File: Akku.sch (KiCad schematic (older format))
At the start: 45 parts, among them J1 +/- Stecker, J2 load/up, J3 down/en/clear, P7 CONN_02X10, P8 CONN_02X10, P9 CONN_02X10, SW1 UP_Bonsai_SWITCH_INV, SW2 DOWN_Bonsai_SWITCH_INV, SW3 CLR_Bonsai_SWITCH_INV, U1 74HC14, U2 7400, U4 7408, U5 74LS193, U6 74LS541, U7 74LS193, U8 74LS540

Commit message: akku sch updates for same wireing in pcb
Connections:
- net labels added: CLR, ^down, ^enable, ^load, ûp
- wire segments 226 -> 245
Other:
- moved on the sheet: D1, J2, J3, R9

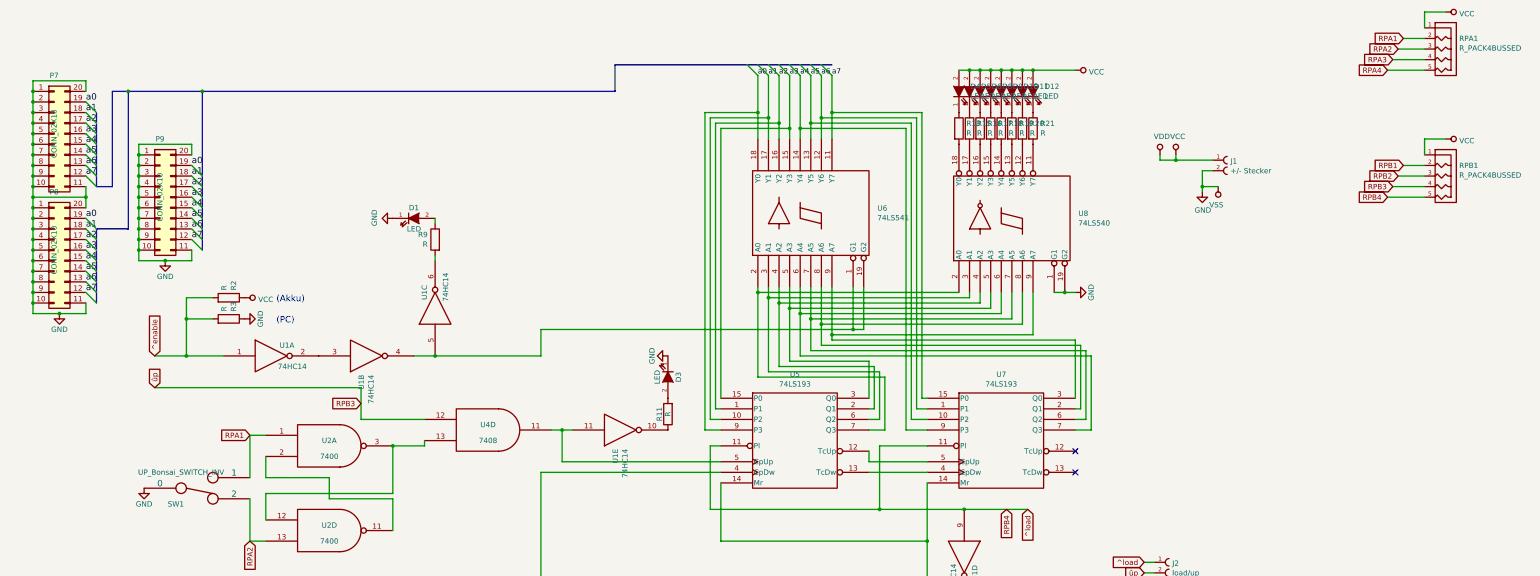
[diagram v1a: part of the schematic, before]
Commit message: akku wireing in pcb
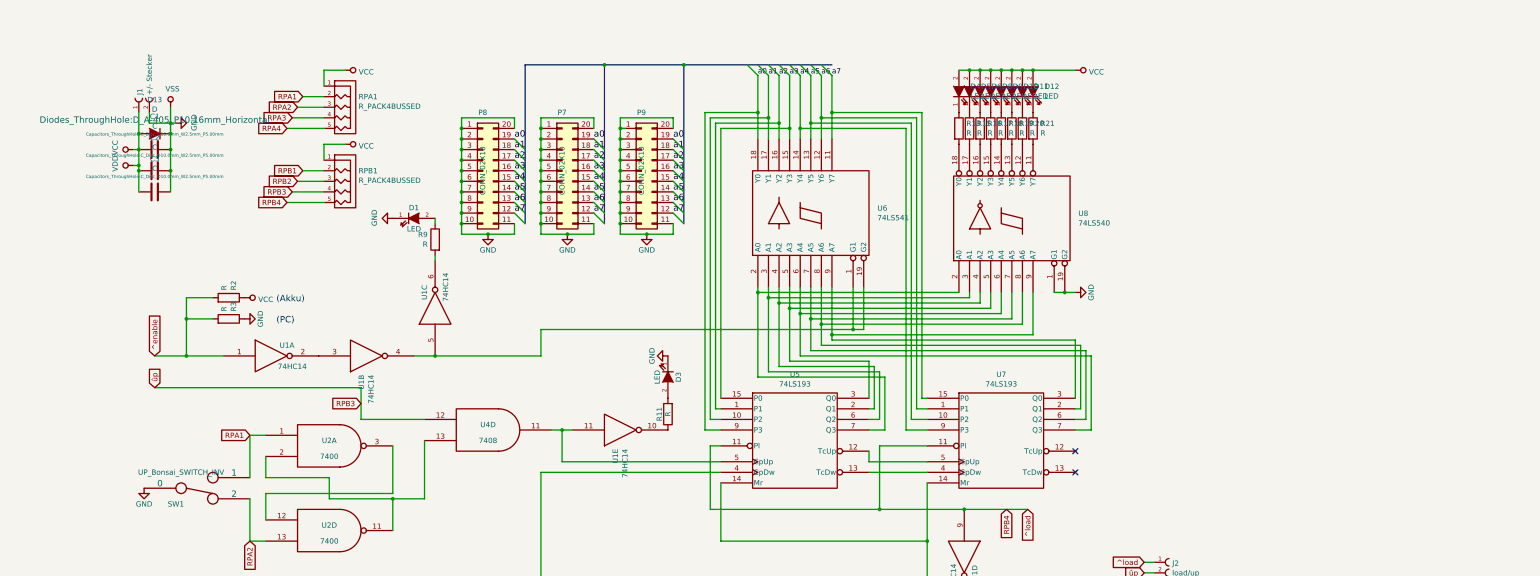
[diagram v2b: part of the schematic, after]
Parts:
- added C1, C2, C3: C, Capacitors_ThroughHole:C_Disc_D10.0mm_W2.5mm_P5.00mm, symbol bonsai:C
- added D13: D, Diodes_ThroughHole:D_A-405_P10.16mm_Horizontal, symbol bonsai:D
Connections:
- net GND: now also C1.1, C2.1, C3.1, D13.1 (K)
- net VCC: now also C1.2, C2.2, C3.2, D13.2 (A)
- net at U2.12, U2.3: no longer U4.13
- net at U2.11, U2.2: now also U4.13
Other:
- moved on the sheet: J1, P7, P8, P9, RPA1, RPB1

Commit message: akku and wireing in pcb
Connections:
- net GND: now also SW3.6
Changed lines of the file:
@@
 Connection ~ 850  1600
 Connection ~ 1150 1600
+$Comp
+L power:GND #PWR?
+U 1 1 5CDAAA47
+P 8000 5950
+F 0 "#PWR?" H 8000 5700 50  0001 C CNN
+F 1 "GND" H 8000 5800 50  0000 C CNN
+F 2 "" H 8000 5950 50  0000 C CNN
+F 3 "" H 8000 5950 50  0000 C CNN
+	1    8000 5950
+	0    -1   -1   0
+$EndComp
 Wire Bus Line
 	5250 600  5250 2100

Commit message: Akku pc finished
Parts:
- C1, C2, C3: footprint Capacitors_ThroughHole:C_Disc_D10.0mm_W2.5mm_P5.00mm -> tg_foodprint:C_Disc_D10.0mm_W2.5mm_P5.00mm
- D13: footprint Diodes_ThroughHole:D_A-405_P10.16mm_Horizontal -> Pin_Headers:D_DO-41_SOD81_P10.16mm_Horizontal
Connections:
- net at U5.12 (TcUp): no longer U7.5 (CpUp)
- net at U5.13 (TcDw): no longer U7.4 (CpDw)
- net at U1.13, U4.3: now also U7.4 (CpDw); no longer U5.4 (CpDw)
- net at U1.11, U4.11: now also U7.5 (CpUp); no longer U5.5 (CpUp)
- net at U7.12 (TcUp): now also U5.5 (CpUp)
- net at U7.13 (TcDw): now also U5.4 (CpDw)
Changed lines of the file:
@@
 Wire Wire Line
 	8300 4550 8300 5100
-Wire Wire Line
-	4650 4450 6350 4450
 Connection ~ 4650 6050
-Wire Wire Line
-	4650 4450 4650 6050
 Wire Wire Line
 	4600 6050 4650 6050
@@
 	8300 5100 6350 5100
 Wire Wire Line
-	7750 4350 7750 4250
-Wire Wire Line
-	8300 4350 7750 4350
-Wire Wire Line
 	6250 4200 6350 4200
 Wire Wire Line
@@
 Wire Wire Line
 	7300 2700 7300 3050
-Wire Wire Line
-	7750 4450 8300 4450
-NoConn ~ 9700 4250
-NoConn ~ 9700 4450
 $Comp
 L Akku-rescue:74HC14-RESCUE-Akku U1
@@
 Connection ~ 9600 2750
 Wire Wire Line
-	6350 4350 4850 4350
-Wire Wire Line
-	4850 4350 4850 4050
+	6350 4350 6050 4350
 Connection ~ 4850 4050
 Wire Wire Line
@@
 F 0 "C1" V 688 1400 50  0000 C CNN
 F 1 "C" V 779 1400 50  0000 C CNN
-F 2 "Capacitors_ThroughHole:C_Disc_D10.0mm_W2.5mm_P5.00mm" V 855 1400 30  0000 C CNN
+F 2 "tg_foodprint:C_Disc_D10.0mm_W2.5mm_P5.00mm" V 855 1400 30  0000 C CNN
 F 3 "" H 1000 1400 60  0000 C CNN
 	1    1000 1400
@@
 F 0 "C2" V 688 1600 50  0000 C CNN
 F 1 "C" V 779 1600 50  0000 C CNN
-F 2 "Capacitors_ThroughHole:C_Disc_D10.0mm_W2.5mm_P5.00mm" V 855 1600 30  0000 C CNN
+F 2 "tg_foodprint:C_Disc_D10.0mm_W2.5mm_P5.00mm" V 855 1600 30  0000 C CNN
 F 3 "" H 1000 1600 60  0000 C CNN
 	1    1000 1600
@@
 F 0 "D13" H 1000 929 50  0000 C CNN
 F 1 "D" H 1000 1020 50  0000 C CNN
-F 2 "Diodes_ThroughHole:D_A-405_P10.16mm_Horizontal" H 1000 1119 60  0000 C CNN
+F 2 "Pin_Headers:D_DO-41_SOD81_P10.16mm_Horizontal" H 1000 1119 60  0000 C CNN
 F 3 "" H 1000 1250 60  0000 C CNN
 	1    1000 1250
@@
 F 0 "C3" V 688 1800 50  0000 C CNN
 F 1 "C" V 779 1800 50  0000 C CNN
-F 2 "Capacitors_ThroughHole:C_Disc_D10.0mm_W2.5mm_P5.00mm" V 855 1800 30  0000 C CNN
+F 2 "tg_foodprint:C_Disc_D10.0mm_W2.5mm_P5.00mm" V 855 1800 30  0000 C CNN
 F 3 "" H 1000 1800 60  0000 C CNN
 	1    1000 1800
@@
 Connection ~ 1150 1600
 $Comp
-L power:GND #PWR?
+L power:GND #PWR0104
 U 1 1 5CDAAA47
 P 8000 5950
-F 0 "#PWR?" H 8000 5700 50  0001 C CNN
+F 0 "#PWR0104" H 8000 5700 50  0001 C CNN
 F 1 "GND" H 8000 5800 50  0000 C CNN
 F 2 "" H 8000 5950 50  0000 C CNN
@@
 	0    -1   -1   0
 $EndComp
+Wire Wire Line
+	9700 4450 9700 4650
+Wire Wire Line
+	9700 4650 6100 4650
+Wire Wire Line
+	6100 4650 6100 4450
+Wire Wire Line
+	9700 4250 9800 4250
+Wire Wire Line
+	9800 4250 9800 4700
+Wire Wire Line
+	8300 4450 8150 4450
+Wire Wire Line
+	8150 4450 8150 5350
+Wire Wire Line
+	8150 5350 4650 5350
+Wire Wire Line
+	4650 5350 4650 6050
+Wire Wire Line
+	6050 4700 6050 4350
+Wire Wire Line
+	9800 4700 6050 4700
+Wire Wire Line
+	8300 4350 8100 4350
+Wire Wire Line
+	8100 4350 8100 5250
+Wire Wire Line
+	8100 5250 4850 5250
+Wire Wire Line
+	4850 4050 4850 5250
+NoConn ~ 7750 4250
+NoConn ~ 7750 4450
+Wire Wire Line
+	6350 4450 6100 4450
+Wire Bus Line
+	6000 600  7400 600
+Wire Bus Line
+	4500 600  4500 2100
 Wire Bus Line
 	5250 600  5250 2100
 Wire Bus Line
-	4500 600  4500 2100
-Wire Bus Line
 	6000 600  6000 2100
-Wire Bus Line
-	6000 600  7400 600
 $EndSCHEMATC

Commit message: Eintakt libs fixed
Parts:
- C1, C2, C3: symbol bonsai:C -> Akku-rescue:C-bonsai-Akku-rescue
- D1, D10, D11, D12, D2, D3, D4, D5, D6, D7, D8, D9: symbol bonsai:LED -> Akku-rescue:LED-bonsai-Akku-rescue
- D13: symbol bonsai:D -> Akku-rescue:D-bonsai-Akku-rescue
- J1, J2: symbol Akku-rescue:2PinTerminalBlocktg-2PinTerminalBlocktg -> Akku-rescue:2PinTerminalBlocktg-2PinTerminalBlocktg-Akku-rescue-Akku-rescue
- J3: symbol Akku-rescue:3PinTerminalBlocktg-3PinTerminalBlocktg -> Akku-rescue:3PinTerminalBlocktg-3PinTerminalBlocktg-Akku-rescue-Akku-rescue
- P7, P8, P9: symbol Akku-rescue:Conn_02x10_Counter_Clockwise-conn -> Akku-rescue:Conn_02x10_Counter_Clockwise-conn-Akku-rescue-Akku-rescue
- R10, R11, R12, R13, R14, R15, R16, R17, R18, R19, R2, R20, R21, R3, R9: symbol Akku-rescue:R-device -> Akku-rescue:R-device-Akku-rescue-Akku-rescue
- RPA1, RPB1: symbol bonsai:R_PACK4BUSSED -> Akku-rescue:R_PACK4BUSSED-bonsai-Akku-rescue
- SW1, SW2, SW3: symbol bonsai:SWITCH_INV -> Akku-rescue:SWITCH_INV-bonsai-Akku-rescue
- U1: symbol Akku-rescue:4069-cmos4000 -> Akku-rescue:4069-cmos4000-Akku-rescue-Akku-rescue
- U1: symbol Akku-rescue:74HC14-RESCUE-Akku -> Akku-rescue:74HC14-RESCUE-Akku-Akku-rescue-Akku-rescue
- U2: symbol Akku-rescue:7400-RESCUE-Akku -> Akku-rescue:7400-RESCUE-Akku-Akku-rescue-Akku-rescue
- U4: symbol Akku-rescue:74LS08-74xx -> Akku-rescue:74LS08-74xx-Akku-rescue-Akku-rescue
- U5, U7: symbol Akku-rescue:74LS193-RESCUE-Akku -> Akku-rescue:74LS193-RESCUE-Akku-Akku-rescue-Akku-rescue
- U6: symbol Akku-rescue:74LS541-74xx -> Akku-rescue:74LS541-74xx-Akku-rescue-Akku-rescue
- U8: symbol Akku-rescue:74LS540-74xx -> Akku-rescue:74LS540-74xx-Akku-rescue-Akku-rescue
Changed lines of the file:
@@
 Akkumulator
 $Comp
-L Akku-rescue:74LS540-74xx U8
+L Akku-rescue:74LS540-74xx-Akku-rescue-Akku-rescue U8
 U 1 1 57E93AAD
 P 9100 2050
@@
 $EndComp
 $Comp
-L bonsai:LED D12
+L Akku-rescue:LED-bonsai-Akku-rescue D12
 U 1 1 57E93BF0
 P 9300 850
@@
 $EndComp
 $Comp
-L bonsai:LED D11
+L Akku-rescue:LED-bonsai-Akku-rescue D11
 U 1 1 57E93CED
 P 9200 850
@@
 $EndComp
 $Comp
-L bonsai:LED D10
+L Akku-rescue:LED-bonsai-Akku-rescue D10
 U 1 1 57E93ED1
 P 9100 850
@@
 $EndComp
 $Comp
-L bonsai:LED D9
+L Akku-rescue:LED-bonsai-Akku-rescue D9
 U 1 1 57E93F38
 P 9000 850
@@
 $EndComp
 $Comp
-L bonsai:LED D8
+L Akku-rescue:LED-bonsai-Akku-rescue D8
 U 1 1 57E93F7E
 P 8900 850
@@
 $EndComp
 $Comp
-L bonsai:LED D6
+L Akku-rescue:LED-bonsai-Akku-rescue D6
 U 1 1 57E93FA3
 P 8800 850
@@
 $EndComp
 $Comp
-L bonsai:LED D5
+L Akku-rescue:LED-bonsai-Akku-rescue D5
 U 1 1 57E93FCF
 P 8700 850
@@
 $EndComp
 $Comp
-L bonsai:LED D4
+L Akku-rescue:LED-bonsai-Akku-rescue D4
 U 1 1 57E93FFA
 P 8600 850
@@
 $EndComp
 $Comp
-L Akku-rescue:R-device R13
+L Akku-rescue:R-device-Akku-rescue-Akku-rescue R13
 U 1 1 57E94162
 P 8600 1200
@@
 $EndComp
 $Comp
-L Akku-rescue:R-device R15
+L Akku-rescue:R-device-Akku-rescue-Akku-rescue R15
 U 1 1 57E942DE
 P 8700 1200
@@
 $EndComp
 $Comp
-L Akku-rescue:R-device R16
+L Akku-rescue:R-device-Akku-rescue-Akku-rescue R16
 U 1 1 57E94316
 P 8800 1200
@@
 $EndComp
 $Comp
-L Akku-rescue:R-device R17
+L Akku-rescue:R-device-Akku-rescue-Akku-rescue R17
 U 1 1 57E94362
 P 8900 1200
@@
 $EndComp
 $Comp
-L Akku-rescue:R-device R18
+L Akku-rescue:R-device-Akku-rescue-Akku-rescue R18
 U 1 1 57E943BA
 P 9000 1200
@@
 $EndComp
 $Comp
-L Akku-rescue:R-device R19
+L Akku-rescue:R-device-Akku-rescue-Akku-rescue R19
 U 1 1 57E94424
 P 9100 1200
@@
 $EndComp
 $Comp
-L Akku-rescue:R-device R20
+L Akku-rescue:R-device-Akku-rescue-Akku-rescue R20
 U 1 1 57E94464
 P 9200 1200
@@
 $EndComp
 $Comp
-L Akku-rescue:R-device R21
+L Akku-rescue:R-device-Akku-rescue-Akku-rescue R21
 U 1 1 57E944B7
 P 9300 1200
@@
 $EndComp
 $Comp
-L Akku-rescue:74LS193-RESCUE-Akku U5
+L Akku-rescue:74LS193-RESCUE-Akku-Akku-rescue-Akku-rescue U5
 U 1 1 57E9530E
 P 7050 4150
@@
 $EndComp
 $Comp
-L Akku-rescue:74LS193-RESCUE-Akku U7
+L Akku-rescue:74LS193-RESCUE-Akku-Akku-rescue-Akku-rescue U7
 U 1 1 57E95727
 P 9000 4150
@@
 $EndComp
 $Comp
-L Akku-rescue:R-device R14
+L Akku-rescue:R-device-Akku-rescue-Akku-rescue R14
 U 1 1 57E98213
 P 8650 5850
@@
 $EndComp
 $Comp
-L Akku-rescue:R-device R9
+L Akku-rescue:R-device-Akku-rescue-Akku-rescue R9
 U 1 1 57F2FBEB
 P 3650 2250
@@
 $EndComp
 $Comp
-L bonsai:LED D7
+L Akku-rescue:LED-bonsai-Akku-rescue D7
 U 1 1 57FBC65C
 P 8850 6000
@@
 $EndComp
 $Comp
-L Akku-rescue:R-device R12
+L Akku-rescue:R-device-Akku-rescue-Akku-rescue R12
 U 1 1 57FC1E29
 P 8150 6200
@@
 $EndComp
 $Comp
-L bonsai:SWITCH_INV SW3
+L Akku-rescue:SWITCH_INV-bonsai-Akku-rescue SW3
 U 1 1 57FC34DF
 P 7500 6200
@@
 $EndComp
 $Comp
-L Akku-rescue:74LS541-74xx U6
+L Akku-rescue:74LS541-74xx-Akku-rescue-Akku-rescue U6
 U 1 1 57E939A0
 P 7200 2000
@@
 $EndComp
 $Comp
-L Akku-rescue:Conn_02x10_Counter_Clockwise-conn P7
+L Akku-rescue:Conn_02x10_Counter_Clockwise-conn-Akku-rescue-Akku-rescue P7
 U 1 1 58057A43
 P 4850 1600
@@
 $EndComp
 $Comp
-L Akku-rescue:Conn_02x10_Counter_Clockwise-conn P8
+L Akku-rescue:Conn_02x10_Counter_Clockwise-conn-Akku-rescue-Akku-rescue P8
 U 1 1 5805867B
 P 4100 1600
@@
 $EndComp
 $Comp
-L Akku-rescue:Conn_02x10_Counter_Clockwise-conn P9
+L Akku-rescue:Conn_02x10_Counter_Clockwise-conn-Akku-rescue-Akku-rescue P9
 U 1 1 58058F42
 P 5600 1600
@@
 $EndComp
 $Comp
-L bonsai:LED D1
+L Akku-rescue:LED-bonsai-Akku-rescue D1
 U 1 1 580EE5C2
 P 3450 2050
@@
 $EndComp
 $Comp
-L Akku-rescue:4069-cmos4000 U1
+L Akku-rescue:4069-cmos4000-Akku-rescue-Akku-rescue U1
 U 2 1 580F11C5
 P 3000 3350
@@
 $EndComp
 $Comp
-L Akku-rescue:R-device R2
+L Akku-rescue:R-device-Akku-rescue-Akku-rescue R2
 U 1 1 580F178A
 P 1700 2800
@@
 $EndComp
 $Comp
-L Akku-rescue:R-device R3
+L Akku-rescue:R-device-Akku-rescue-Akku-rescue R3
 U 1 1 580F350E
 P 1700 3000
@@
 (PC)
 $Comp
-L Akku-rescue:74LS08-74xx U4
+L Akku-rescue:74LS08-74xx-Akku-rescue-Akku-rescue U4
 U 4 1 580F517F
 P 4150 4050
@@
 $EndComp
 $Comp
-L Akku-rescue:7400-RESCUE-Akku U2
+L Akku-rescue:7400-RESCUE-Akku-Akku-rescue-Akku-rescue U2
 U 4 1 580F5956
 P 2650 5000
@@
 $EndComp
 $Comp
-L Akku-rescue:7400-RESCUE-Akku U2
+L Akku-rescue:7400-RESCUE-Akku-Akku-rescue-Akku-rescue U2
 U 1 1 580F5818
 P 2650 4200
@@
 $EndComp
 $Comp
-L bonsai:SWITCH_INV SW1
+L Akku-rescue:SWITCH_INV-bonsai-Akku-rescue SW1
 U 1 1 58100CBF
 P 1400 4600
@@
 $EndComp
 $Comp
-L Akku-rescue:4069-cmos4000 U1
+L Akku-rescue:4069-cmos4000-Akku-rescue-Akku-rescue U1
 U 5 1 581014B6
 P 5400 4050
@@
 $EndComp
 $Comp
-L Akku-rescue:R-device R11
+L Akku-rescue:R-device-Akku-rescue-Akku-rescue R11
 U 1 1 581018B2
 P 5850 3900
@@
 $EndComp
 $Comp
-L bonsai:LED D3
+L Akku-rescue:LED-bonsai-Akku-rescue D3
 U 1 1 58101E2D
 P 5850 3550
@@
 $EndComp
 $Comp
-L Akku-rescue:7400-RESCUE-Akku U2
+L Akku-rescue:7400-RESCUE-Akku-Akku-rescue-Akku-rescue U2
 U 3 1 58103E9D
 P 2650 5950
@@
 $EndComp
 $Comp
-L Akku-rescue:7400-RESCUE-Akku U2
+L Akku-rescue:7400-RESCUE-Akku-Akku-rescue-Akku-rescue U2
 U 2 1 58103EA3
 P 2650 6750
@@
 $EndComp
 $Comp
-L bonsai:SWITCH_INV SW2
+L Akku-rescue:SWITCH_INV-bonsai-Akku-rescue SW2
 U 1 1 58103EB5
 P 1400 6350
@@
 $EndComp
 $Comp
-L Akku-rescue:74LS08-74xx U4
+L Akku-rescue:74LS08-74xx-Akku-rescue-Akku-rescue U4
 U 1 1 581052DF
 P 4000 6050
@@
 	7300 2700 7300 3050
 $Comp
-L Akku-rescue:74HC14-RESCUE-Akku U1
+L Akku-rescue:74HC14-RESCUE-Akku-Akku-rescue-Akku-rescue U1
 U 1 1 5A159C74
 P 2100 3350
@@
 $EndComp
 $Comp
-L Akku-rescue:74HC14-RESCUE-Akku U1
+L Akku-rescue:74HC14-RESCUE-Akku-Akku-rescue-Akku-rescue U1
 U 3 1 5A159ED2
 P 3650 2900
@@
 $EndComp
 $Comp
-L Akku-rescue:74HC14-RESCUE-Akku U1
+L Akku-rescue:74HC14-RESCUE-Akku-Akku-rescue-Akku-rescue U1
 U 6 1 5A15A24E
 P 5200 6050
@@
 $EndComp
 $Comp
-L Akku-rescue:74HC14-RESCUE-Akku U1
+L Akku-rescue:74HC14-RESCUE-Akku-Akku-rescue-Akku-rescue U1
 U 4 1 5A15A4DE
 P 8650 5250
@@
 	850  1400 800  1400
 $Comp
-L Akku-rescue:2PinTerminalBlocktg-2PinTerminalBlocktg J1
+L Akku-rescue:2PinTerminalBlocktg-2PinTerminalBlocktg-Akku-rescue-Akku-rescue J1
 U 1 1 5AECBED9
 P 850 850
@@
 $EndComp
 $Comp
-L Akku-rescue:2PinTerminalBlocktg-2PinTerminalBlocktg J2
+L Akku-rescue:2PinTerminalBlocktg-2PinTerminalBlocktg-Akku-rescue-Akku-rescue J2
 U 1 1 5AECC155
 P 10650 5300
@@
 $EndComp
 $Comp
-L Akku-rescue:3PinTerminalBlocktg-3PinTerminalBlocktg J3
+L Akku-rescue:3PinTerminalBlocktg-3PinTerminalBlocktg-Akku-rescue-Akku-rescue J3
 U 1 1 5AECC360
 P 10650 5650
@@
 	1150 1150 1200 1150
 $Comp
-L bonsai:R_PACK4BUSSED RPA1
+L Akku-rescue:R_PACK4BUSSED-bonsai-Akku-rescue RPA1
 U 1 1 5B220C3D
 P 2800 1000
@@
 $EndComp
 $Comp
-L Akku-rescue:R-device R10
+L Akku-rescue:R-device-Akku-rescue-Akku-rescue R10
 U 1 1 5810516E
 P 5650 6200
@@
 $EndComp
 $Comp
-L bonsai:LED D2
+L Akku-rescue:LED-bonsai-Akku-rescue D2
 U 1 1 58105174
 P 5650 6550
@@
 RPA3
 $Comp
-L bonsai:R_PACK4BUSSED RPB1
+L Akku-rescue:R_PACK4BUSSED-bonsai-Akku-rescue RPB1
 U 1 1 5B22DE13
 P 2800 1700
@@
 Connection ~ 6000 600
 $Comp
-L bonsai:C C1
+L Akku-rescue:C-bonsai-Akku-rescue C1
 U 1 1 5CBF3D2E
 P 1000 1400
 F 0 "C1" V 688 1400 50  0000 C CNN
 F 1 "C" V 779 1400 50  0000 C CNN
-F 2 "tg_foodprint:C_Disc_D10.0mm_W2.5mm_P5.00mm" V 855 1400 30  0000 C CNN
+F 2 "tg_foodprint:C_Disc_D10.0mm_W2.5mm_P5.00mm" V 855 1400 30  0001 C CNN
 F 3 "" H 1000 1400 60  0000 C CNN
 	1    1000 1400
@@
 $EndComp
 $Comp
-L bonsai:C C2
+L Akku-rescue:C-bonsai-Akku-rescue C2
 U 1 1 5CBF52E5
 P 1000 1600
 F 0 "C2" V 688 1600 50  0000 C CNN
 F 1 "C" V 779 1600 50  0000 C CNN
-F 2 "tg_foodprint:C_Disc_D10.0mm_W2.5mm_P5.00mm" V 855 1600 30  0000 C CNN
+F 2 "tg_foodprint:C_Disc_D10.0mm_W2.5mm_P5.00mm" V 855 1600 30  0001 C CNN
 F 3 "" H 1000 1600 60  0000 C CNN
 	1    1000 1600
@@
 $EndComp
 $Comp
-L bonsai:D D13
+L Akku-rescue:D-bonsai-Akku-rescue D13
 U 1 1 5CC05CEA
 P 1000 1250
 F 0 "D13" H 1000 929 50  0000 C CNN
 F 1 "D" H 1000 1020 50  0000 C CNN
-F 2 "Pin_Headers:D_DO-41_SOD81_P10.16mm_Horizontal" H 1000 1119 60  0000 C CNN
+F 2 "Pin_Headers:D_DO-41_SOD81_P10.16mm_Horizontal" H 1000 1119 60  0001 C CNN
 F 3 "" H 1000 1250 60  0000 C CNN
 	1    1000 1250
@@
 Connection ~ 850  1550
 $Comp
-L bonsai:C C3
+L Akku-rescue:C-bonsai-Akku-rescue C3
 U 1 1 5CC7F388
 P 1000 1800
 F 0 "C3" V 688 1800 50  0000 C CNN
 F 1 "C" V 779 1800 50  0000 C CNN
-F 2 "tg_foodprint:C_Disc_D10.0mm_W2.5mm_P5.00mm" V 855 1800 30  0000 C CNN
+F 2 "tg_foodprint:C_Disc_D10.0mm_W2.5mm_P5.00mm" V 855 1800 30  0001 C CNN
 F 3 "" H 1000 1800 60  0000 C CNN
 	1    1000 1800
